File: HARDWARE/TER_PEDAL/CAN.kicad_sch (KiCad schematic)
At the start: 7 parts, among them U4 SN65HVD230

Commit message: Added Uniport, Debug and began sensors design
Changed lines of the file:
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@@
     (effects (font (size 1.27 1.27)) (justify right))
   )
-  (hierarchical_label "CAN-" (shape input) (at 200.66 86.36 0) (fields_autoplaced)
+  (hierarchical_label "CAN-" (shape bidirectional) (at 200.66 86.36 0) (fields_autoplaced)
     (effects (font (size 1.27 1.27)) (justify left))
   )
-  (hierarchical_label "CAN+" (shape input) (at 200.66 82.55 0) (fields_autoplaced)
+  (hierarchical_label "CAN+" (shape bidirectional) (at 200.66 82.55 0) (fields_autoplaced)
     (effects (font (size 1.27 1.27)) (justify left))
   )

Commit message: Added footprints to existing components
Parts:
- C17, C18: footprint (none) -> Capacitor_SMD:C_0603_1608Metric
- JP3: footprint (none) -> Jumper:SolderJumper-3_P1.3mm_Open_Pad1.0x1.5mm
- R8, R9: footprint (none) -> Resistor_SMD:R_0603_1608Metric
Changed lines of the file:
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@@
       (effects (font (size 1.27 1.27)))
     )
-    (property "Footprint" "" (at 144.78 82.8548 0)
+    (property "Footprint" "Capacitor_SMD:C_0603_1608Metric" (at 144.78 82.8548 0)
       (effects (font (size 1.27 1.27)) hide)
     )
@@
       (effects (font (size 1.27 1.27)) (justify left))
     )
-    (property "Footprint" "" (at 156.21 83.82 0)
+    (property "Footprint" "Jumper:SolderJumper-3_P1.3mm_Open_Pad1.0x1.5mm" (at 156.21 83.82 0)
       (effects (font (size 1.27 1.27)) hide)
     )
@@
       (effects (font (size 1.27 1.27)) (justify left))
     )
-    (property "Footprint" "" (at 156.21 76.2 0)
+    (property "Footprint" "Resistor_SMD:R_0603_1608Metric" (at 156.21 76.2 0)
       (effects (font (size 1.27 1.27)) hide)
     )
@@
       (effects (font (size 1.27 1.27)) (justify left))
     )
-    (property "Footprint" "" (at 156.21 92.71 0)
+    (property "Footprint" "Resistor_SMD:R_0603_1608Metric" (at 156.21 92.71 0)
       (effects (font (size 1.27 1.27)) hide)
     )
@@
       (effects (font (size 1.27 1.27)))
     )
-    (property "Footprint" "" (at 93.98 66.3448 0)
-      (effects (font (size 1.27 1.27)) hide)
-    )
+    (property "Footprint" "Capacitor_SMD:C_0603_1608Metric" (at 93.98 66.3448 0)
+      (effects (font (size 1.27 1.27)) hide)
+    )

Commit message: Sized and Fixed even more footprints + Initial layout
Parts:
- R8, R9: value 60R -> 50R
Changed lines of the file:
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@@
       (effects (font (size 1.27 1.27)) (justify left))
     )
-    (property "Value" "60R" (at 158.75 78.105 0)
+    (property "Value" "50R" (at 158.75 78.105 0)
       (effects (font (size 1.27 1.27)) (justify left))
     )
@@
       (effects (font (size 1.27 1.27)) (justify left))
     )
-    (property "Value" "60R" (at 158.75 94.615 0)
+    (property "Value" "50R" (at 158.75 94.615 0)
       (effects (font (size 1.27 1.27)) (justify left))
     )

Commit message: Cabiado esquematico, falta layout
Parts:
- removed C17: 100n, Capacitor_SMD:C_0603_1608Metric, symbol Device:C
- removed C18: 4.7n, Capacitor_SMD:C_0603_1608Metric, symbol Device:C
- removed JP3: TermEnable, Jumper:SolderJumper-3_P1.3mm_Open_Pad1.0x1.5mm, symbol Jumper:SolderJumper_3_Open
- removed R8, R9: 50R, Resistor_SMD:R_0603_1608Metric, symbol Device:R_Small
- added C31: 100nF, Capacitor_SMD:C_0603_1608Metric, symbol Device:C
- added C32: 4.7nF, Capacitor_SMD:C_0603_1608Metric, symbol Device:C
- added FL2: ACT45B-510-2P-TL003, ACT45B-510-2P-TL003:FIL_ACT45B-510-2P-TL003, symbol CAN_CMF:ACT45B-510-2P-TL003
- added JP2: SolderJumper_3_Open, Jumper:SolderJumper-3_P1.3mm_Open_Pad1.0x1.5mm, symbol Jumper:SolderJumper_3_Open
- added R32, R9: 50R, Resistor_SMD:R_0805_2012Metric, symbol Device:R
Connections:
- net +3.3V: now also C31.2
- net CAN+: now also FL2.2, R9.1; no longer D2.1 (K), U4.7 (CANH)
- net CAN-: now also FL2.1, R32.2; no longer D2.2 (K), U4.6 (CANL)
- net GND: now also C31.1, C32.2
- net VREF: now also C32.1, JP2.2 (C)
- new net: JP2.1 (A), R9.2
- new net: JP2.3 (B), R32.1
- new net: D2.1 (K), FL2.4, U4.6 (CANL)
- new net: D2.2 (K), FL2.3, U4.7 (CANH)
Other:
- note added: "Isolated Can Bus transceiver"
- note removed: "La terminación split del can crea un filtro RC por encima de 1Mhz"

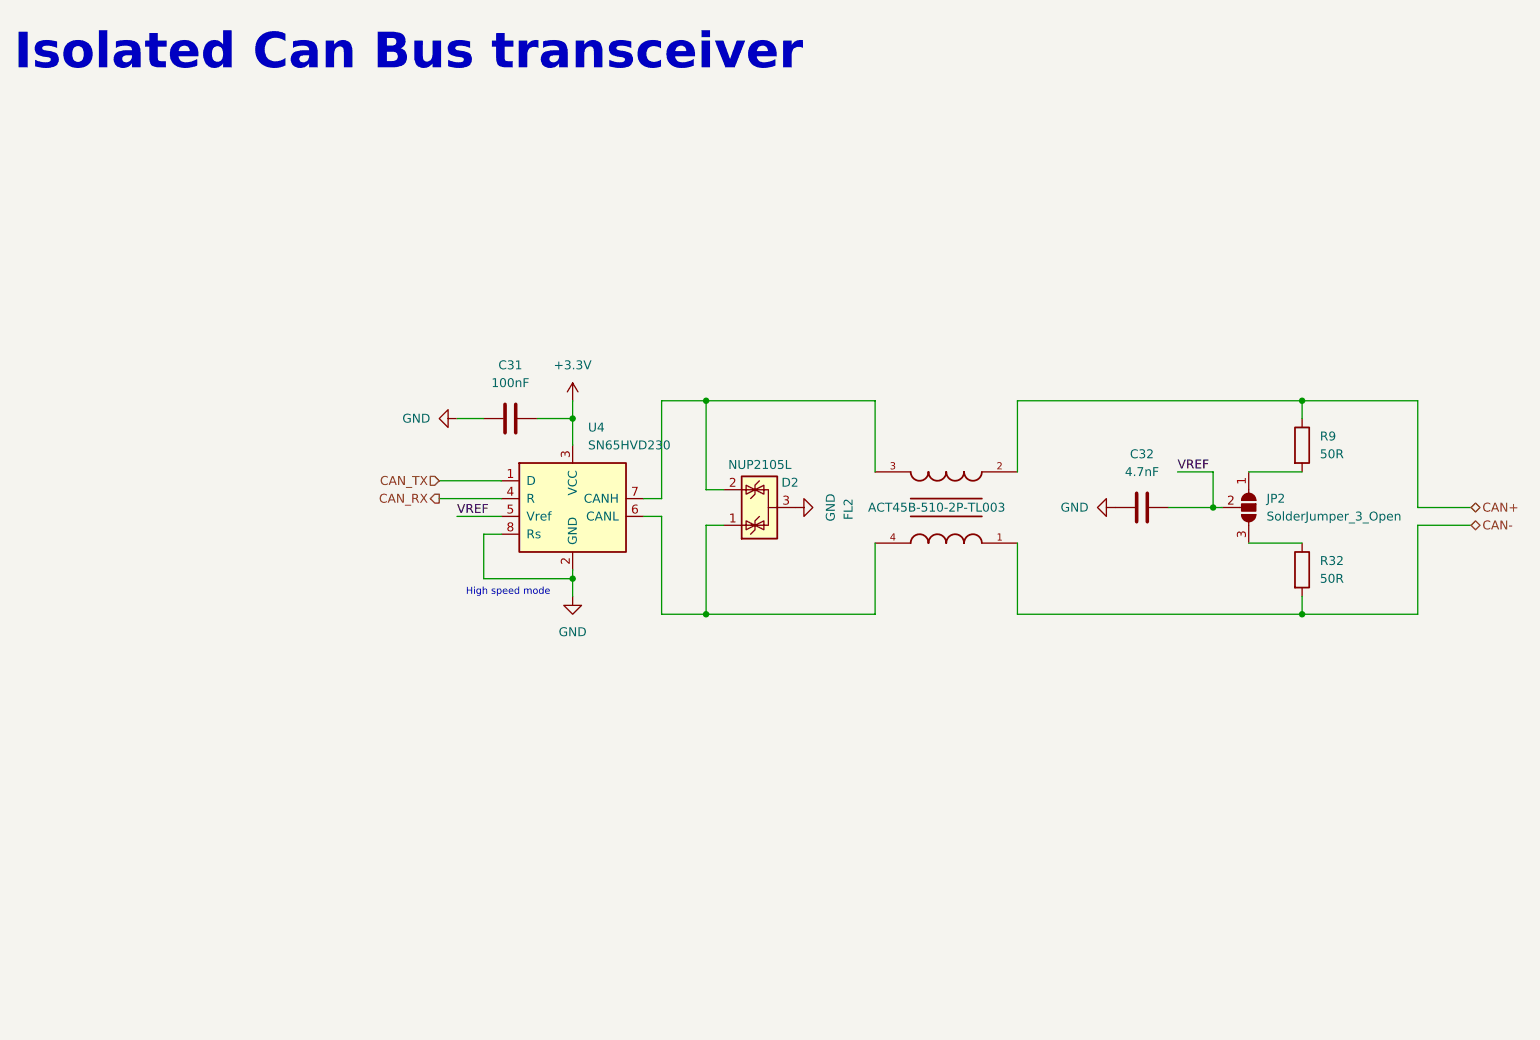
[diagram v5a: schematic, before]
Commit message: Added voltage followers to sensing, improved can circuitri, improved layout, waiting for routing
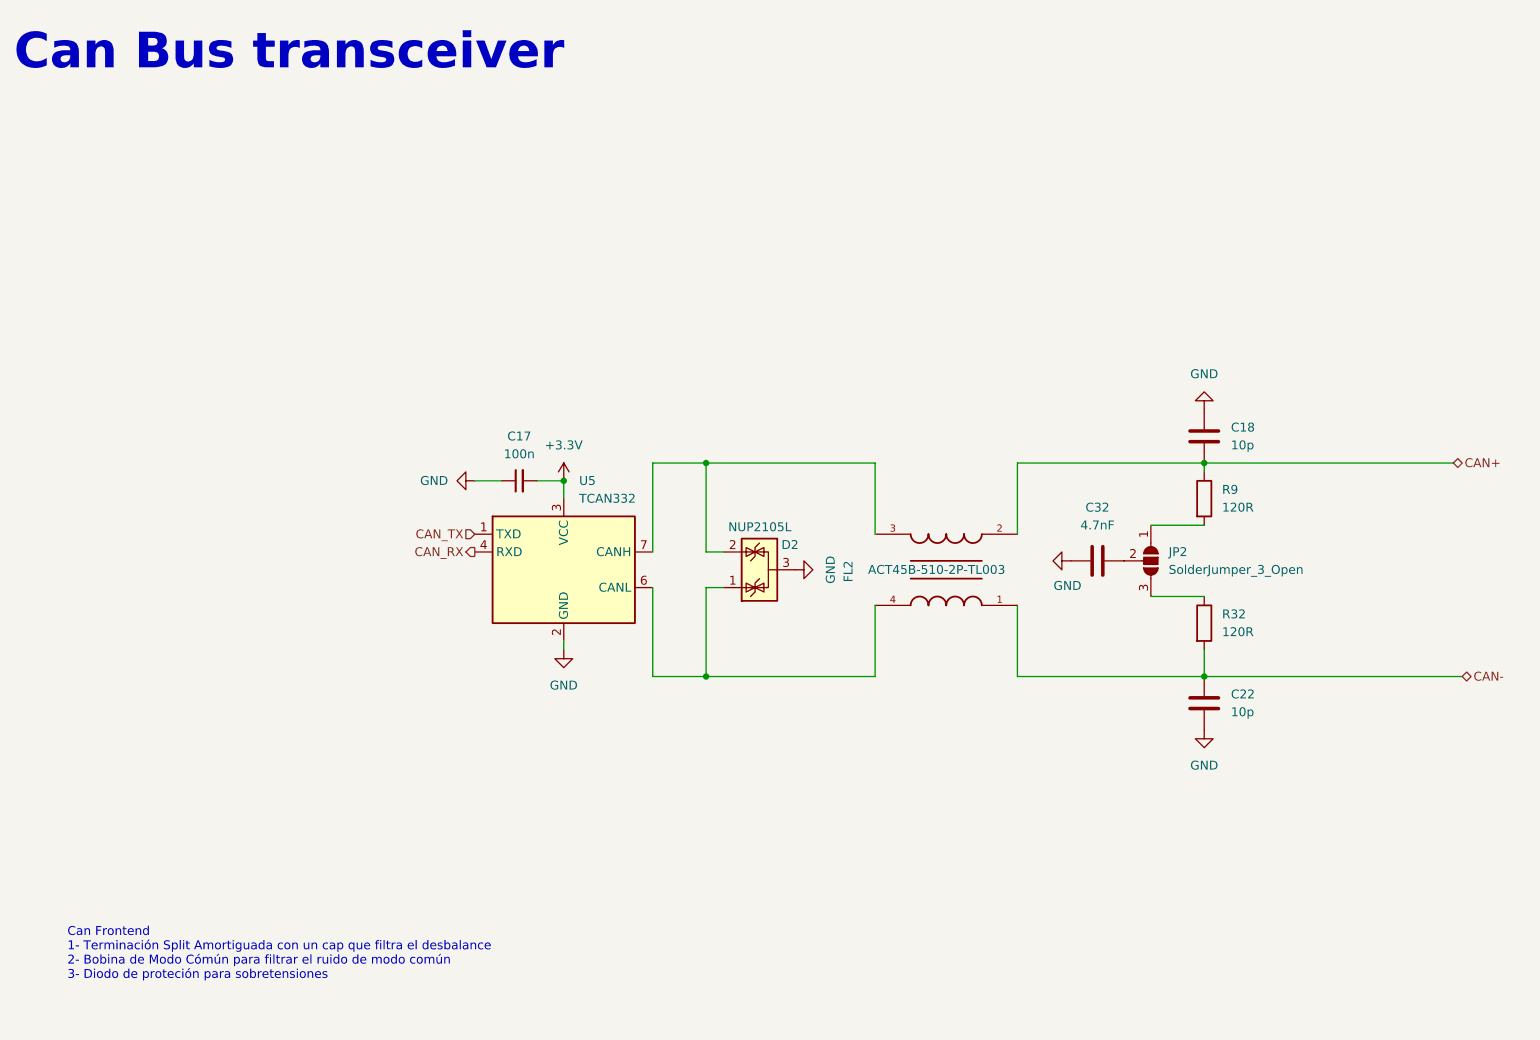
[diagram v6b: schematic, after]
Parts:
- removed C31: 100nF, Capacitor_SMD:C_0603_1608Metric, symbol Device:C
- removed U4: SN65HVD230, Package_SO:SOIC-8_3.9x4.9mm_P1.27mm, symbol Interface_CAN_LIN:SN65HVD230
- added C17: 100n, Capacitor_SMD:C_0603_1608Metric, symbol Device:C_Small
- added C18, C22: 10p, Capacitor_SMD:C_0603_1608Metric, symbol Device:C
- added U5: TCAN332, Package_SO:SOIC-8_3.9x4.9mm_P1.27mm, symbol Interface_CAN_LIN:TCAN332
- R32, R9: value 50R -> 120R; footprint Resistor_SMD:R_0805_2012Metric -> Resistor_SMD:R_0603_1608Metric
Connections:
- net +3.3V: now also C17.2, U5.3 (VCC)
- net CAN+: now also C18.2
- net CAN-: now also C22.1
- net CAN_RX: now also U5.4 (RXD)
- net CAN_TX: now also U5.1 (TXD)
- net GND: now also C17.1, C18.1, C22.2, U5.2 (GND)
- net at D2.1 (K), FL2.4: now also U5.6 (CANL)
- net at D2.2 (K), FL2.3: now also U5.7 (CANH)
- net VREF: no longer names the net of C32.1, JP2.2 (C)
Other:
- note added: "Can Bus transceiver"
- note added: "Can Frontend 1- Terminación Split Amortiguada con un cap que filtra el desbalance 2- Bobina de Modo Cómún para filtrar el ruido de modo común 3- Diodo de proteción para sobretensiones"
- note removed: "High speed mode"
- note removed: "Isolated Can Bus transceiver"
- company: (none) -> Tecnun-eRacing
- title: (none) -> TeR_PEDAL
- moved on the sheet: C32, D2, FL2, JP2, R32, R9

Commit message: avanzando layout
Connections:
- net can-: now reaches D2.1 (K), FL2.4, U5.6 (CANL)
- net can+: now reaches D2.2 (K), FL2.3, U5.7 (CANH)
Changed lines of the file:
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@@
+		)
+	)
+	(label "can+"
+		(at 121.92 80.01 0)
+		(fields_autoplaced yes)
+		(effects
+			(font
+				(size 1.27 1.27)
+			)
+			(justify left bottom)
+		)
+	)
+	(label "can-"
+		(at 123.19 110.49 0)
+		(fields_autoplaced yes)
+		(effects
+			(font
+				(size 1.27 1.27)
+			)
+			(justify left bottom)
 		)
 	)
